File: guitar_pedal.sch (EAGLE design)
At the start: 98 parts, among them P1 RM-065, P2 RM-065, P3 RM-065, U1 LM324NSOIC-14, U2 LM324NSOIC-14, U3 LM386N-3, U4 LM386N-3, U5 LM386N-3

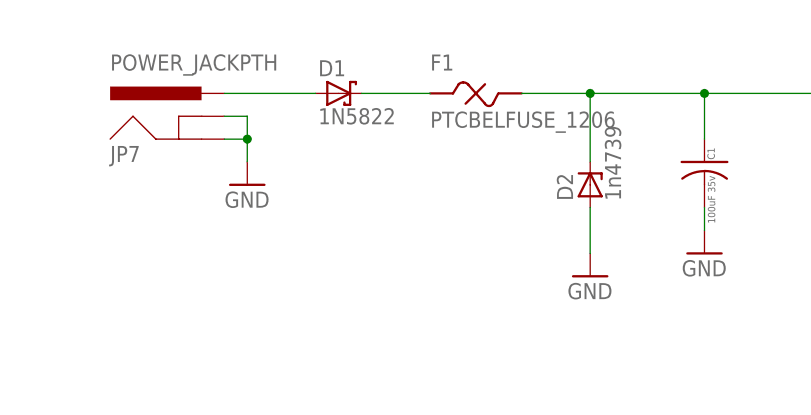
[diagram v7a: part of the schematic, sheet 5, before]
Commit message: changed PTC to tayda 1.1A through hole component.
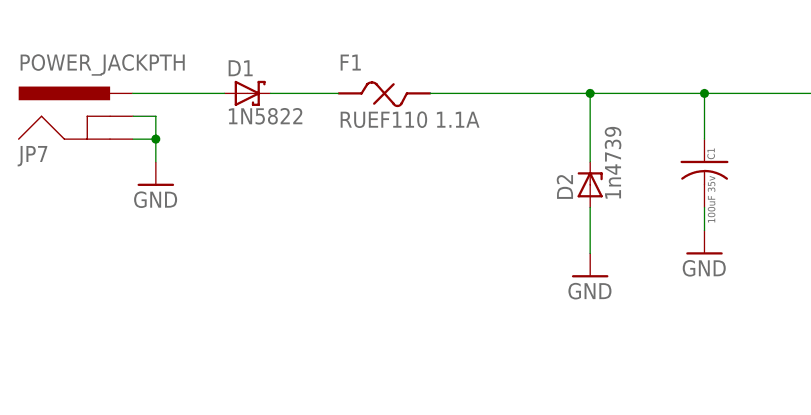
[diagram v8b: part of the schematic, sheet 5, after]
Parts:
- F1: value PTCBELFUSE_1206 -> RUEF110 1.1A; device Luke:PTCBELFUSE_1206 -> Luke:PTCRUEF110
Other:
- moved on the sheet: D1, F1, JP7
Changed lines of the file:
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@@
 <part name="R42" library="aarons" deviceset="POT" device="" value="500k"/>
 <part name="C21" library="Luke" deviceset="CAP_CAN01" device="" value="470uF"/>
-<part name="F1" library="Luke" deviceset="PTC" device="BELFUSE_1206"/>
+<part name="F1" library="Luke" deviceset="PTC" device="RUEF110" value="RUEF110 1.1A"/>
 <part name="C27" library="Luke" deviceset="CAPACITOR" device="0805" value="1uF"/>
 <part name="C28" library="Luke" deviceset="CAPACITOR" device="0805" value="1uF"/>
@@
 </plain>
 <instances>
-<instance part="JP7" gate="G$1" x="86.36" y="114.3"/>
-<instance part="GND1" gate="1" x="91.44" y="111.76"/>
-<instance part="D1" gate="G$1" x="101.6" y="121.92"/>
+<instance part="JP7" gate="G$1" x="76.2" y="114.3"/>
+<instance part="GND1" gate="1" x="81.28" y="111.76"/>
+<instance part="D1" gate="G$1" x="91.44" y="121.92"/>
 <instance part="D2" gate="G$1" x="129.54" y="111.76" rot="R90"/>
 <instance part="GND8" gate="1" x="129.54" y="101.6"/>
@@
 <instance part="C1" gate="G$1" x="142.24" y="114.3"/>
 <instance part="C2" gate="G$1" x="157.48" y="114.3"/>
-<instance part="F1" gate="G$1" x="116.84" y="121.92"/>
+<instance part="F1" gate="G$1" x="106.68" y="121.92"/>
 <instance part="C34" gate="G$1" x="182.88" y="99.06"/>
 <instance part="GND40" gate="1" x="182.88" y="91.44"/>
@@
 <segment>
 <pinref part="JP7" gate="G$1" pin="GNDBREAK"/>
-<wire x1="88.9" y1="119.38" x2="91.44" y2="119.38" width="0.1524" layer="91"/>
-<wire x1="91.44" y1="119.38" x2="91.44" y2="116.84" width="0.1524" layer="91"/>
+<wire x1="78.74" y1="119.38" x2="81.28" y2="119.38" width="0.1524" layer="91"/>
+<wire x1="81.28" y1="119.38" x2="81.28" y2="116.84" width="0.1524" layer="91"/>
 <pinref part="JP7" gate="G$1" pin="GND"/>
-<wire x1="91.44" y1="116.84" x2="88.9" y2="116.84" width="0.1524" layer="91"/>
-<wire x1="91.44" y1="116.84" x2="91.44" y2="114.3" width="0.1524" layer="91"/>
-<junction x="91.44" y="116.84"/>
+<wire x1="81.28" y1="116.84" x2="78.74" y2="116.84" width="0.1524" layer="91"/>
+<wire x1="81.28" y1="116.84" x2="81.28" y2="114.3" width="0.1524" layer="91"/>
+<junction x="81.28" y="116.84"/>
 <pinref part="GND1" gate="1" pin="GND"/>
 </segment>
@@
 <segment>
 <pinref part="JP7" gate="G$1" pin="PWR"/>
-<wire x1="88.9" y1="121.92" x2="99.06" y2="121.92" width="0.1524" layer="91"/>
+<wire x1="78.74" y1="121.92" x2="88.9" y2="121.92" width="0.1524" layer="91"/>
 <pinref part="D1" gate="G$1" pin="A"/>
 </segment>
@@
 <pinref part="SUPPLY1" gate="G$1" pin="+9V"/>
 <junction x="172.72" y="121.92"/>
-<wire x1="121.92" y1="121.92" x2="129.54" y2="121.92" width="0.1524" layer="91"/>
+<wire x1="111.76" y1="121.92" x2="129.54" y2="121.92" width="0.1524" layer="91"/>
 <junction x="129.54" y="121.92"/>
 <pinref part="C1" gate="G$1" pin="POS"/>
@@
 <segment>
 <pinref part="D1" gate="G$1" pin="C"/>
-<wire x1="104.14" y1="121.92" x2="111.76" y2="121.92" width="0.1524" layer="91"/>
+<wire x1="93.98" y1="121.92" x2="101.6" y2="121.92" width="0.1524" layer="91"/>
 <pinref part="F1" gate="G$1" pin="1"/>
 </segment>
